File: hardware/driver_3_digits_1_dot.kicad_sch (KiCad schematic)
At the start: 12 parts, among them U4 HV5622PG

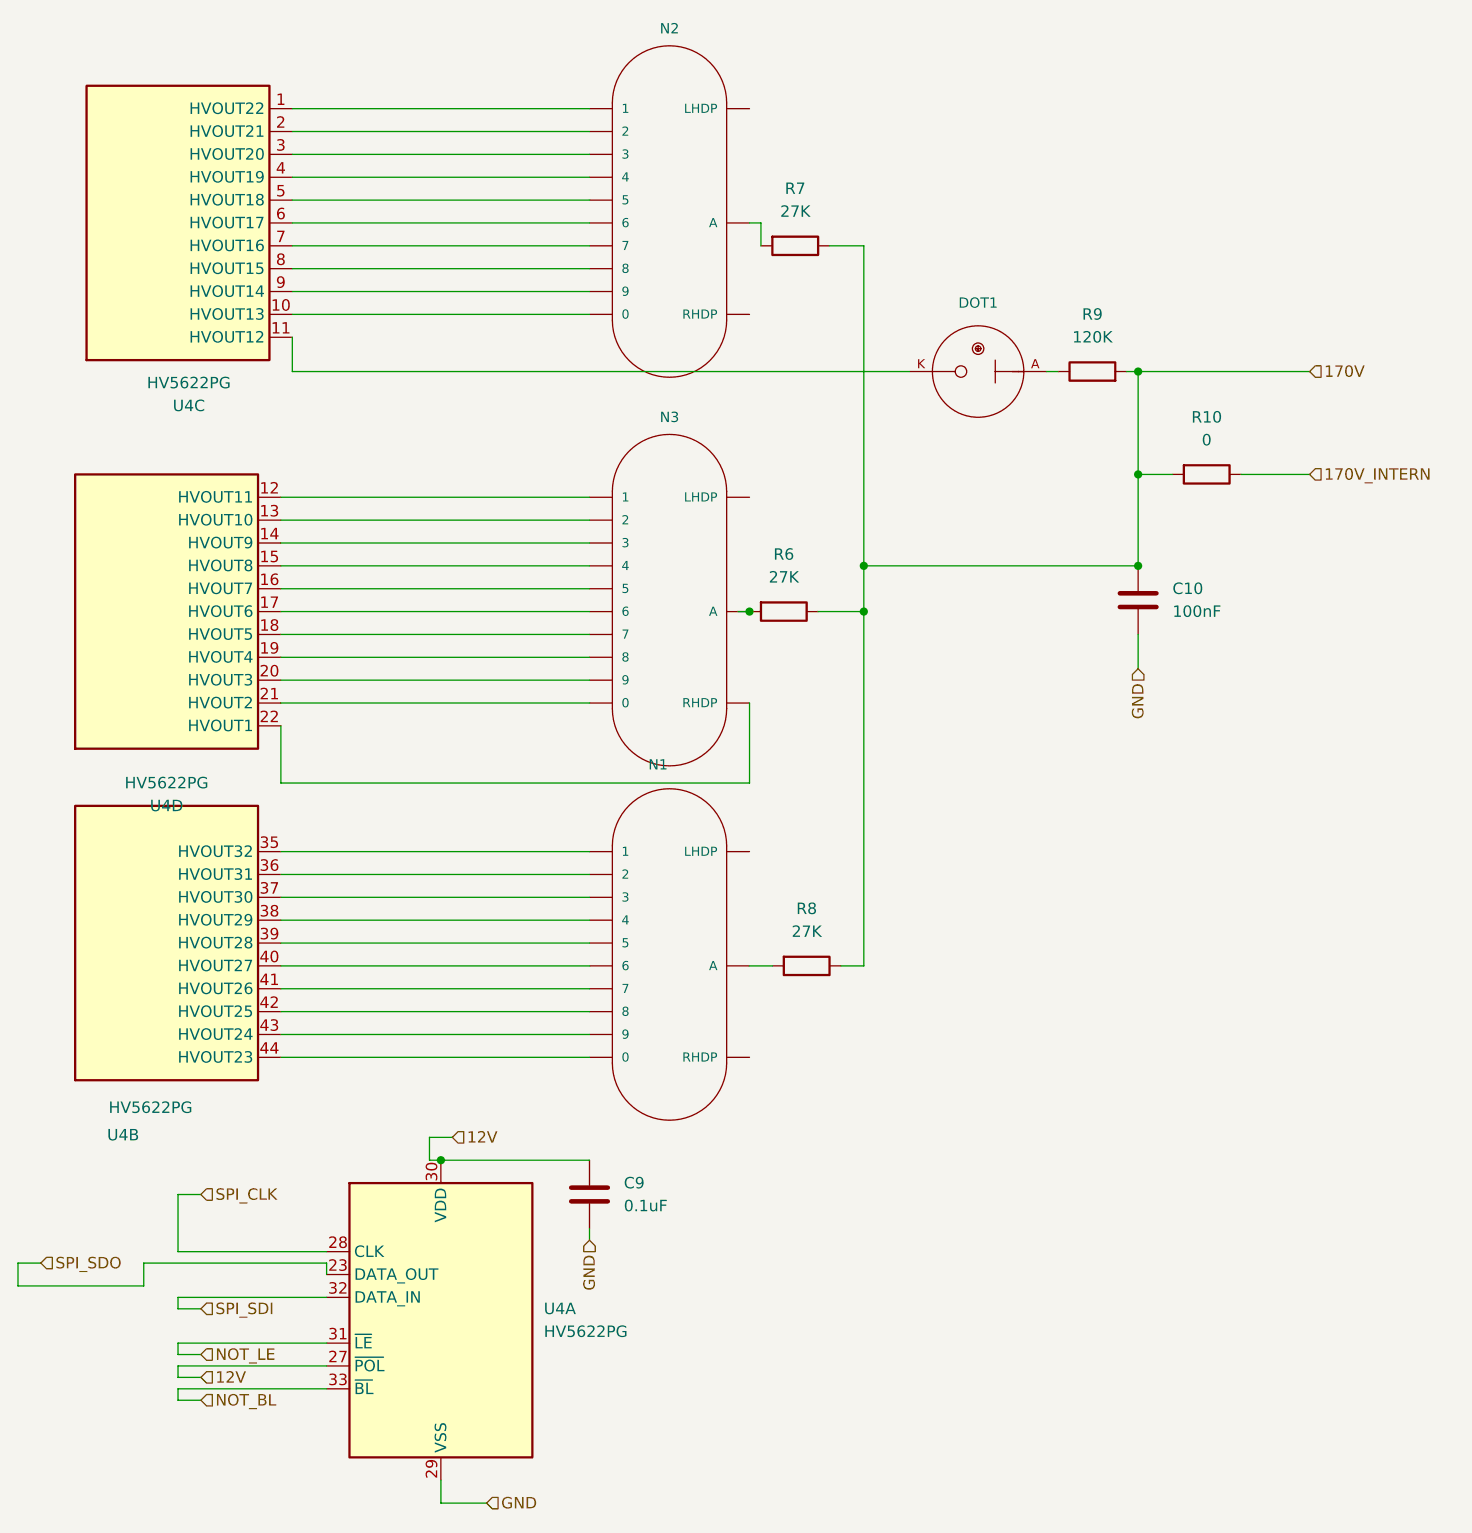
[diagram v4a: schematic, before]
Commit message: Rework  3.3v power supply (fix error on fb loop). Put 1206 back on HV part.
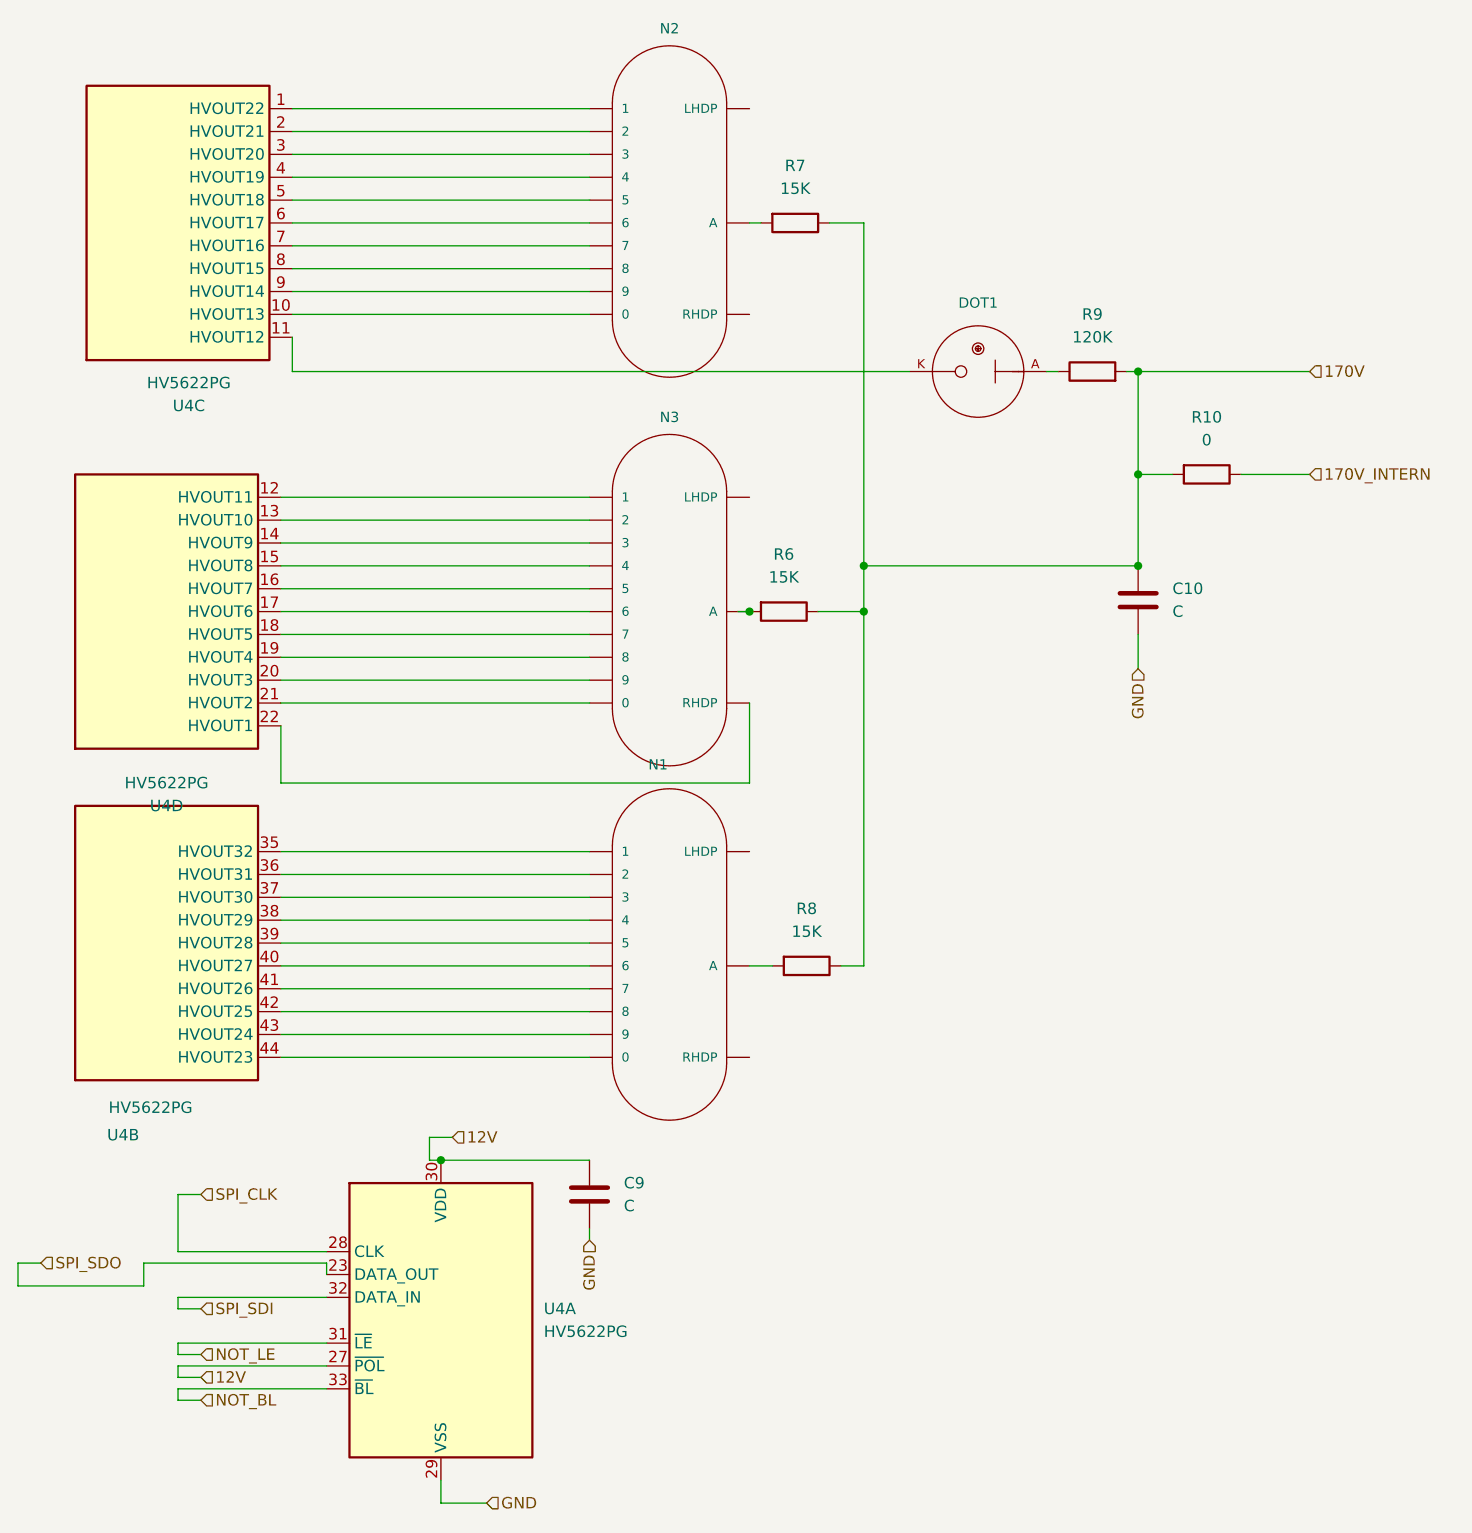
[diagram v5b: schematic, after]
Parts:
- C10: value 100nF -> C
- C9: value 0.1uF -> C
- DOT1: footprint nixies-us:nixies-us-IN-3 -> nixies-us_IN-3
- N1, N2, N3: footprint nixies-us:nixies-us-IN-14 -> nixies-us_IN-14
- R6, R7, R8: value 27K -> 15K
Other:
- moved on the sheet: R7
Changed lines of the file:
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@@
 	(wire
 		(pts
-			(xy 148.59 46.99) (xy 152.4 46.99)
+			(xy 148.59 44.45) (xy 152.4 44.45)
 		)
 		(stroke
@@
 	(wire
 		(pts
-			(xy 140.97 44.45) (xy 140.97 46.99)
-		)
-		(stroke
-			(width 0)
-			(type default)
-		)
-	)
-	(wire
-		(pts
 			(xy 88.9 52.07) (xy 121.92 52.07)
 		)
@@
 	(wire
 		(pts
-			(xy 152.4 46.99) (xy 152.4 82.55)
+			(xy 152.4 44.45) (xy 152.4 82.55)
 		)
 		(stroke
@@
 			)
 		)
-		(property "Footprint" "nixies-us:nixies-us-IN-3"
+		(property "Footprint" "nixies-us_IN-3"
 			(at 169.418 54.61 0)
 			(effects
@@
 	(symbol
 		(lib_id "Device:R")
-		(at 144.78 46.99 270)
+		(at 144.78 44.45 270)
 		(unit 1)
 		(exclude_from_sim no)
@@
 		(fields_autoplaced yes)
 		(property "Reference" "R7"
+			(at 144.78 38.1 90)
+			(effects
+				(font
+					(size 1.27 1.27)
+				)
+			)
+		)
+		(property "Value" "15K"
 			(at 144.78 40.64 90)
 			(effects
@@
 			)
 		)
-		(property "Value" "27K"
-			(at 144.78 43.18 90)
-			(effects
-				(font
-					(size 1.27 1.27)
-				)
-			)
-		)
 		(property "Footprint" "Resistor_SMD:R_1206_3216Metric"
-			(at 144.78 45.212 90)
+			(at 144.78 42.672 90)
 			(effects
 				(font
@@
 		)
 		(property "Datasheet" "~"
-			(at 144.78 46.99 0)
+			(at 144.78 44.45 0)
 			(effects
 				(font
@@
 		)
 		(property "Description" "Resistor"
-			(at 144.78 46.99 0)
+			(at 144.78 44.45 0)
 			(effects
 				(font
@@
 			)
 		)
-		(property "Value" "27K"
+		(property "Value" "15K"
 			(at 146.05 123.19 90)
 			(effects
@@
 			)
 		)
-		(property "Footprint" "nixies-us:nixies-us-IN-14"
+		(property "Footprint" "nixies-us_IN-14"
 			(at 130.302 38.1 0)
 			(effects
@@
 		(exclude_from_sim no)
 		(in_bom yes)
-		(on_board yes)
+		(on_board no)
 		(dnp no)
 		(fields_autoplaced yes)
@@
 			)
 		)
-		(property "Value" "27K"
+		(property "Value" "15K"
 			(at 143.51 83.82 90)
 			(effects
@@
 			)
 		)
-		(property "Footprint" "nixies-us:nixies-us-IN-14"
+		(property "Footprint" "nixies-us_IN-14"
 			(at 130.302 81.28 0)
 			(effects
@@
 			)
 		)
-		(property "Footprint" "nixies-us:nixies-us-IN-14"
+		(property "Footprint" "nixies-us_IN-14"
 			(at 130.302 120.65 0)
 			(effects
@@
 			)
 		)
-		(property "Value" "100nF"
+		(property "Value" "C"
 			(at 186.69 87.6299 0)
 			(effects
@@
 			)
 		)
-		(property "Value" "0.1uF"
+		(property "Value" "C"
 			(at 125.73 153.6699 0)
 			(effects

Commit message: Fix DRC errors.
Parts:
- DOT1: footprint nixies-us_IN-3 -> nixies-us:nixies-us-IN-3
- N1, N2, N3: footprint nixies-us_IN-14 -> nixies-us:nixies-us-IN-14
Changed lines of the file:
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@@
 			)
 		)
-		(property "Footprint" "nixies-us_IN-3"
+		(property "Footprint" "nixies-us:nixies-us-IN-3"
 			(at 169.418 54.61 0)
 			(effects
@@
 			)
 		)
-		(property "Footprint" "nixies-us_IN-14"
+		(property "Footprint" "nixies-us:nixies-us-IN-14"
 			(at 130.302 38.1 0)
 			(effects
@@
 			)
 		)
-		(property "Footprint" "nixies-us_IN-14"
+		(property "Footprint" "nixies-us:nixies-us-IN-14"
 			(at 130.302 81.28 0)
 			(effects
@@
 			)
 		)
-		(property "Footprint" "nixies-us_IN-14"
+		(property "Footprint" "nixies-us:nixies-us-IN-14"
 			(at 130.302 120.65 0)
 			(effects
